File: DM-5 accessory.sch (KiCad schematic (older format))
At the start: 18 parts, among them J1 24VAC, J2 Input, J3 Output, U1 LR645N3

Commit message: respin
better foorprints, single sided board
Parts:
- C1: value 1.0 uF -> 10.0 uF 63V; footprint Capacitors_THT:C_Axial_L5.1mm_D3.1mm_P7.50mm_Horizontal -> Capacitors_THT:CP_Radial_D10.0mm_P2.50mm_P5.00mm
- C2: value .1 uF -> 1.0 uF 63V; footprint Capacitors_THT:C_Disc_D3.8mm_W2.6mm_P2.50mm -> Capacitors_THT:CP_Radial_D10.0mm_P2.50mm_P5.00mm
- D1, D2, D3, D4: footprint Diodes_THT:D_A-405_P7.62mm_Horizontal -> Diodes_THT:D_DO-35_SOD27_P10.16mm_Horizontal
- F1: value 1A 250V -> 1A ATC; footprint Fuse_Holders_and_Fuses:Fuseholder_ATO_Blade_littlefuse_Pudenz_2_Pin -> Fuse_Holders_and_Fuses:BladeFuse-CarType
- F2: value Polyfuse 0.08A -> Polyfuse 6mA; footprint Varistors:RV_Disc_D7_W3.4_P5 -> Varistors:RV_Disc_D7_W4.8_P5
- J1, J3: footprint Connectors_Terminal_Blocks:TerminalBlock_4UCON_19963_02x3.5mm_Straight -> Connectors_Terminal_Blocks:TerminalBlock_Pheonix_PT-3.5mm_2pol
- J2: footprint Connectors_Terminal_Blocks:TerminalBlock_4UCON_19963_04x3.5mm_Straight -> Connectors_Terminal_Blocks:TerminalBlock_Pheonix_PT-3.5mm_4pol
- R1, R2, R3, R4, R5, R6: footprint Resistors_THT:R_Axial_DIN0204_L3.6mm_D1.6mm_P5.08mm_Horizontal -> Resistors_THT:R_Axial_DIN0207_L6.3mm_D2.5mm_P7.62mm_Horizontal
- U1: footprint TO_SOT_Packages_THT:TO-92_Inline_Narrow_Oval -> TO_SOT_Packages_THT:TO-220-3_Vertical
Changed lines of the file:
@@
 F 0 "R1" V 6280 3500 50  0000 C CNN
 F 1 "20K" V 6200 3500 50  0000 C CNN
-F 2 "Resistors_THT:R_Axial_DIN0204_L3.6mm_D1.6mm_P5.08mm_Horizontal" V 6130 3500 50  0001 C CNN
+F 2 "Resistors_THT:R_Axial_DIN0207_L6.3mm_D2.5mm_P7.62mm_Horizontal" V 6130 3500 50  0001 C CNN
 F 3 "" H 6200 3500 50  0001 C CNN
 	1    6200 3500
@@
 F 0 "R2" V 6280 4100 50  0000 C CNN
 F 1 "20K" V 6200 4100 50  0000 C CNN
-F 2 "Resistors_THT:R_Axial_DIN0204_L3.6mm_D1.6mm_P5.08mm_Horizontal" V 6130 4100 50  0001 C CNN
+F 2 "Resistors_THT:R_Axial_DIN0207_L6.3mm_D2.5mm_P7.62mm_Horizontal" V 6130 4100 50  0001 C CNN
 F 3 "" H 6200 4100 50  0001 C CNN
 	1    6200 4100
@@
 F 0 "R4" V 6980 3500 50  0000 C CNN
 F 1 "20K" V 6900 3500 50  0000 C CNN
-F 2 "Resistors_THT:R_Axial_DIN0204_L3.6mm_D1.6mm_P5.08mm_Horizontal" V 6830 3500 50  0001 C CNN
+F 2 "Resistors_THT:R_Axial_DIN0207_L6.3mm_D2.5mm_P7.62mm_Horizontal" V 6830 3500 50  0001 C CNN
 F 3 "" H 6900 3500 50  0001 C CNN
 	1    6900 3500
@@
 F 0 "R6" V 7680 3500 50  0000 C CNN
 F 1 "20K" V 7600 3500 50  0000 C CNN
-F 2 "Resistors_THT:R_Axial_DIN0204_L3.6mm_D1.6mm_P5.08mm_Horizontal" V 7530 3500 50  0001 C CNN
+F 2 "Resistors_THT:R_Axial_DIN0207_L6.3mm_D2.5mm_P7.62mm_Horizontal" V 7530 3500 50  0001 C CNN
 F 3 "" H 7600 3500 50  0001 C CNN
 	1    7600 3500
@@
 F 0 "R3" V 6630 3800 50  0000 C CNN
 F 1 "10K" V 6550 3800 50  0000 C CNN
-F 2 "Resistors_THT:R_Axial_DIN0204_L3.6mm_D1.6mm_P5.08mm_Horizontal" V 6480 3800 50  0001 C CNN
+F 2 "Resistors_THT:R_Axial_DIN0207_L6.3mm_D2.5mm_P7.62mm_Horizontal" V 6480 3800 50  0001 C CNN
 F 3 "" H 6550 3800 50  0001 C CNN
 	1    6550 3800
@@
 F 0 "R5" V 7330 3800 50  0000 C CNN
 F 1 "10K" V 7250 3800 50  0000 C CNN
-F 2 "Resistors_THT:R_Axial_DIN0204_L3.6mm_D1.6mm_P5.08mm_Horizontal" V 7180 3800 50  0001 C CNN
+F 2 "Resistors_THT:R_Axial_DIN0207_L6.3mm_D2.5mm_P7.62mm_Horizontal" V 7180 3800 50  0001 C CNN
 F 3 "" H 7250 3800 50  0001 C CNN
 	1    7250 3800
@@
 P 3850 4350
 F 0 "C1" H 3875 4450 50  0000 L CNN
-F 1 "1.0 uF" H 3875 4250 50  0000 L CNN
-F 2 "Capacitors_THT:C_Axial_L5.1mm_D3.1mm_P7.50mm_Horizontal" H 3888 4200 50  0001 C CNN
+F 1 "10.0 uF 63V" H 3875 4250 50  0000 L CNN
+F 2 "Capacitors_THT:CP_Radial_D10.0mm_P2.50mm_P5.00mm" H 3888 4200 50  0001 C CNN
 F 3 "" H 3850 4350 50  0001 C CNN
 	1    3850 4350
@@
 P 5050 4350
 F 0 "C2" H 5075 4450 50  0000 L CNN
-F 1 ".1 uF" H 5075 4250 50  0000 L CNN
-F 2 "Capacitors_THT:C_Disc_D3.8mm_W2.6mm_P2.50mm" H 5088 4200 50  0001 C CNN
+F 1 "1.0 uF 63V" H 5075 4250 50  0000 L CNN
+F 2 "Capacitors_THT:CP_Radial_D10.0mm_P2.50mm_P5.00mm" H 5088 4200 50  0001 C CNN
 F 3 "" H 5050 4350 50  0001 C CNN
 	1    5050 4350
@@
 F 0 "J1" H 2600 3100 50  0001 C CNN
 F 1 "24VAC" V 2700 2950 50  0000 C CNN
-F 2 "Connectors_Terminal_Blocks:TerminalBlock_4UCON_19963_02x3.5mm_Straight" H 2600 3000 50  0001 C CNN
+F 2 "Connectors_Terminal_Blocks:TerminalBlock_Pheonix_PT-3.5mm_2pol" H 2600 3000 50  0001 C CNN
 F 3 "" H 2600 3000 50  0001 C CNN
 	1    2600 3000
@@
 F 0 "J3" H 8750 3900 50  0001 C CNN
 F 1 "Output" V 8850 3750 50  0000 C CNN
-F 2 "Connectors_Terminal_Blocks:TerminalBlock_4UCON_19963_02x3.5mm_Straight" H 8750 3800 50  0001 C CNN
+F 2 "Connectors_Terminal_Blocks:TerminalBlock_Pheonix_PT-3.5mm_2pol" H 8750 3800 50  0001 C CNN
 F 3 "" H 8750 3800 50  0001 C CNN
 	1    8750 3800
@@
 F 0 "J2" H 6200 2550 50  0001 C CNN
 F 1 "Input" V 6300 2300 50  0000 C CNN
-F 2 "Connectors_Terminal_Blocks:TerminalBlock_4UCON_19963_04x3.5mm_Straight" H 6200 2350 50  0001 C CNN
+F 2 "Connectors_Terminal_Blocks:TerminalBlock_Pheonix_PT-3.5mm_4pol" H 6200 2350 50  0001 C CNN
 F 3 "" H 6200 2350 50  0001 C CNN
 	1    6200 2350
@@
 P 2200 3850
 F 0 "F1" V 2280 3850 50  0000 C CNN
-F 1 "1A 250V" V 2125 3850 50  0000 C CNN
-F 2 "Fuse_Holders_and_Fuses:Fuseholder_ATO_Blade_littlefuse_Pudenz_2_Pin" V 2130 3850 50  0001 C CNN
+F 1 "1A ATC" V 2125 3850 50  0000 C CNN
+F 2 "Fuse_Holders_and_Fuses:BladeFuse-CarType" V 2130 3850 50  0001 C CNN
 F 3 "" H 2200 3850 50  0001 C CNN
 	1    2200 3850
@@
 P 5600 3200
 F 0 "F2" V 5500 3200 50  0000 C CNN
-F 1 "Polyfuse 0.08A" V 5700 3200 50  0000 C CNN
-F 2 "Varistors:RV_Disc_D7_W3.4_P5" H 5650 3000 50  0001 L CNN
+F 1 "Polyfuse 6mA" V 5700 3200 50  0000 C CNN
+F 2 "Varistors:RV_Disc_D7_W4.8_P5" H 5650 3000 50  0001 L CNN
 F 3 "" H 5600 3200 50  0001 C CNN
 	1    5600 3200
@@
 F 0 "D2" H 2500 4450 50  0000 C CNN
 F 1 "D" H 2500 4250 50  0000 C CNN
-F 2 "Diodes_THT:D_A-405_P7.62mm_Horizontal" H 2500 4350 50  0001 C CNN
+F 2 "Diodes_THT:D_DO-35_SOD27_P10.16mm_Horizontal" H 2500 4350 50  0001 C CNN
 F 3 "" H 2500 4350 50  0001 C CNN
 	1    2500 4350
@@
 F 0 "D4" H 2800 4450 50  0000 C CNN
 F 1 "D" H 2800 4250 50  0000 C CNN
-F 2 "Diodes_THT:D_A-405_P7.62mm_Horizontal" H 2800 4350 50  0001 C CNN
+F 2 "Diodes_THT:D_DO-35_SOD27_P10.16mm_Horizontal" H 2800 4350 50  0001 C CNN
 F 3 "" H 2800 4350 50  0001 C CNN
 	1    2800 4350
@@
 F 0 "D1" H 2500 4150 50  0000 C CNN
 F 1 "D" H 2500 3950 50  0000 C CNN
-F 2 "Diodes_THT:D_A-405_P7.62mm_Horizontal" H 2500 4050 50  0001 C CNN
+F 2 "Diodes_THT:D_DO-35_SOD27_P10.16mm_Horizontal" H 2500 4050 50  0001 C CNN
 F 3 "" H 2500 4050 50  0001 C CNN
 	1    2500 4050
@@
 F 0 "D3" H 2800 4150 50  0000 C CNN
 F 1 "D" H 2800 3950 50  0000 C CNN
-F 2 "Diodes_THT:D_A-405_P7.62mm_Horizontal" H 2800 4050 50  0001 C CNN
+F 2 "Diodes_THT:D_DO-35_SOD27_P10.16mm_Horizontal" H 2800 4050 50  0001 C CNN
 F 3 "" H 2800 4050 50  0001 C CNN
 	1    2800 4050
@@
 F 0 "U1" H 4200 4125 50  0000 C CNN
 F 1 "LR645N3" H 4375 4125 50  0000 L CNN
-F 2 "TO_SOT_Packages_THT:TO-92_Inline_Narrow_Oval" H 4450 4325 50  0001 C CIN
+F 2 "TO_SOT_Packages_THT:TO-220-3_Vertical" H 4450 4325 50  0001 C CIN
 F 3 "" H 4450 3900 50  0001 C CNN
 	1    4450 3900
@@
 	4850 3800 6400 3800
 $Comp
-L PWR_FLAG #FLG01
+L PWR_FLAG #FLG1
 U 1 1 5A1B629E
 P 3650 3650
-F 0 "#FLG01" H 3650 3725 50  0001 C CNN
+F 0 "#FLG1" H 3650 3725 50  0001 C CNN
 F 1 "PWR_FLAG" H 3650 3800 50  0000 C CNN
 F 2 "" H 3650 3650 50  0001 C CNN

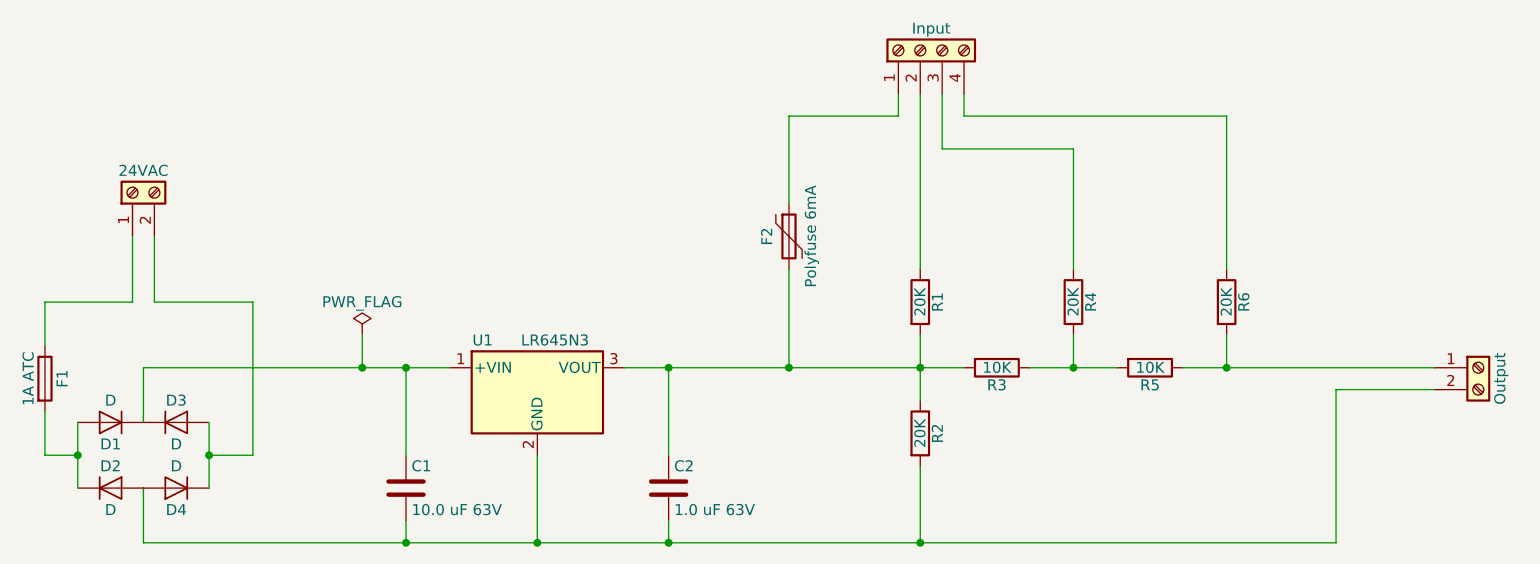
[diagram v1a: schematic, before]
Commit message: respin
swap LR645 -> LR8
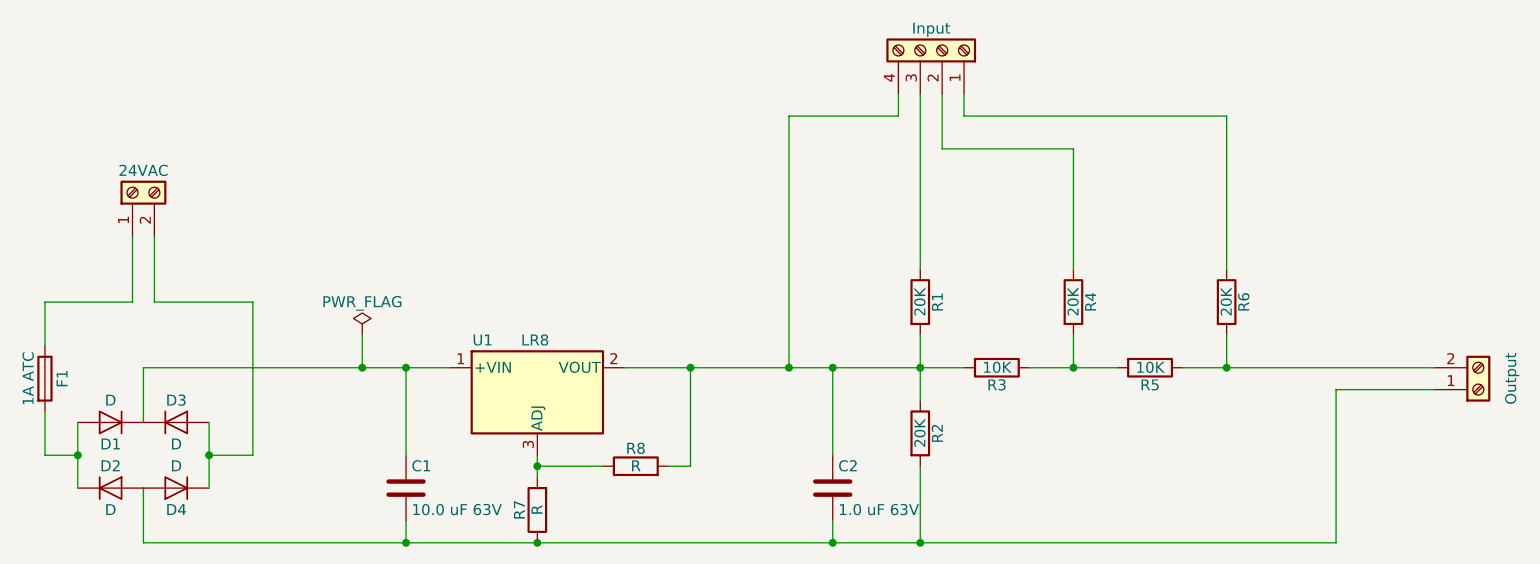
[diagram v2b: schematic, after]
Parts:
- removed F2: Polyfuse 6mA, Varistors:RV_Disc_D7_W4.8_P5, symbol Polyfuse
- removed U1: LR645N3, TO_SOT_Packages_THT:TO-220-3_Vertical, symbol LR645N3
- added R7, R8: R, Resistors_THT:R_Axial_DIN0207_L6.3mm_D2.5mm_P7.62mm_Horizontal, symbol R
- added U1: LR8, TO_SOT_Packages_THT:TO-92_Inline_Narrow_Oval, symbol LR8
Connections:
- net at R1.1: now also J2.3 (Pin_3); no longer J2.2 (Pin_2)
- net at C2.1, R1.2, R2.1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: now also J2.4 (Pin_4), R8.2, U1.2 (VOUT)
- net at C1.2, C2.2, D2.2 (A)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: now also J3.1 (Pin_1), R7.1; no longer J3.2 (Pin_2)
- net at R4.1: now also J2.2 (Pin_2); no longer J2.3 (Pin_3)
- net at R6.1: now also J2.1 (Pin_1); no longer J2.4 (Pin_4)
- net at R5.1, R6.2: now also J3.2 (Pin_2); no longer J3.1 (Pin_1)
- net at C1.1, D1.1 (K), D3.1 (K): now also U1.1 (+VIN)
- new net: R7.2, R8.1, U1.3 (ADJ)
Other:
- moved on the sheet: C2
